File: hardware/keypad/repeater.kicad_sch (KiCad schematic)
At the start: 28 parts, among them Q301 BSS83P, Q302 BSS83P, U301 SN74HCS4075DR, U302 SN74HCS4075DR, U303 SN74HCS4075DR, U304 SN74LVC2G14DBV, U305 LMC555xM, U306 SN74LVC2G14DBVR

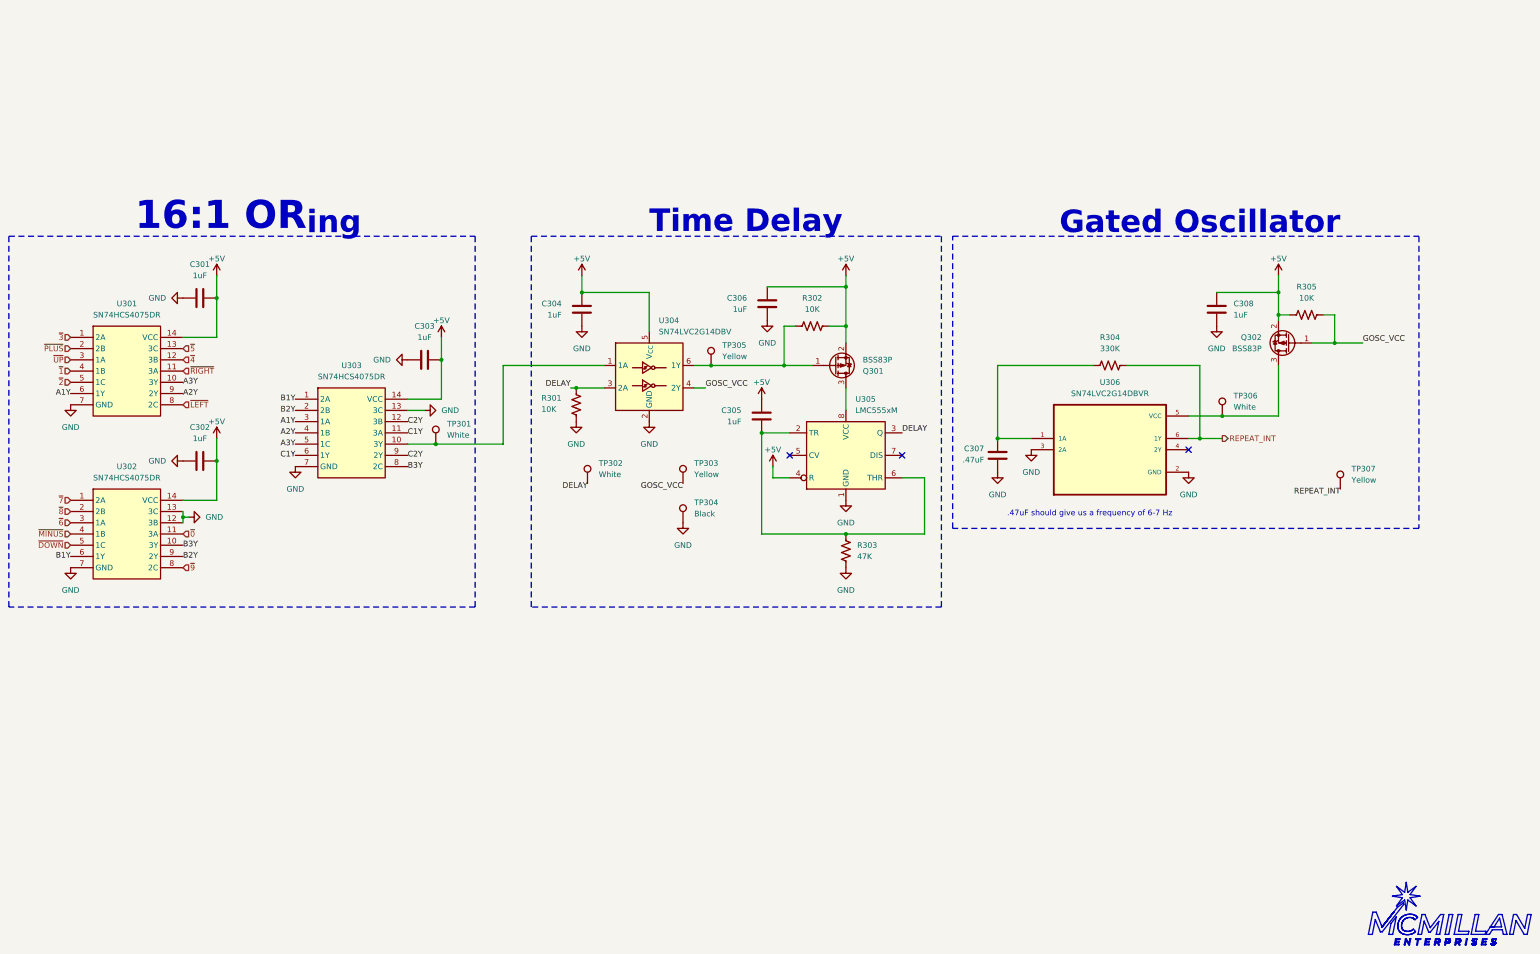
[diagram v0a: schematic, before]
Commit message: Revision X2!
New and improved revision of the keypad! I fixed issues with the repeater and remote SBC power switch circuit (hopefully🤞). I also integrated the Arduino Nano onto the board (ATMEGA328).
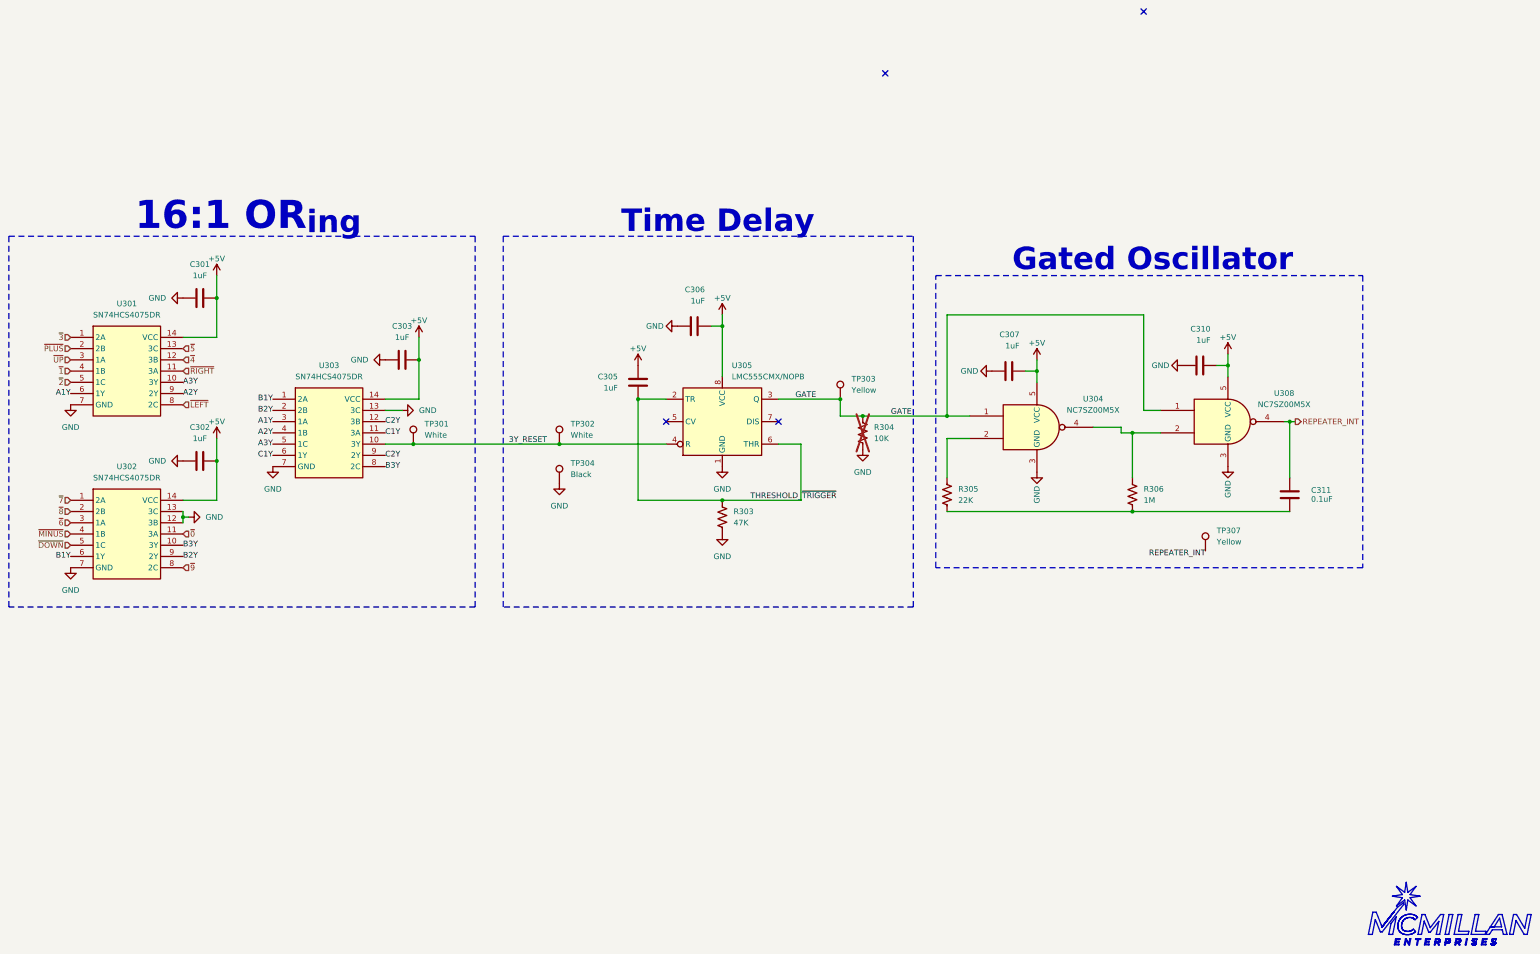
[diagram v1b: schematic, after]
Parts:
- removed C304, C308: 1uF, Capacitor_SMD:C_0805_2012Metric, symbol Device:C
- removed Q301, Q302: BSS83P, Package_TO_SOT_SMD:SOT-23, symbol Transistor_FET:BSS83P
- removed R301, R302: 10K, Resistor_SMD:R_0805_2012Metric, symbol Device:R_US
- removed TP305: Yellow, TestPoint:TestPoint_Keystone_5000-5004_Miniature, symbol Connector:TestPoint
- removed TP306: White, TestPoint:TestPoint_Keystone_5000-5004_Miniature, symbol Connector:TestPoint
- removed U304: SN74LVC2G14DBV, SN74LVC2G14DBVR:SOT95P280X145-6N, symbol 74xGxx:SN74LVC2G14DBV
- removed U306: SN74LVC2G14DBVR, SN74LVC2G14DBVR:SOT95P280X145-6N, symbol SN74LVC2G14DBVR:SN74LVC2G14DBVR
- added C310: 1uF, Capacitor_SMD:C_0805_2012Metric, symbol Device:C
- added C311: 0.1uF, Capacitor_SMD:C_0805_2012Metric, symbol Device:C
- added R306: 1M, Resistor_SMD:R_0805_2012Metric, symbol Device:R_US
- added U304, U308: NC7SZ00M5X, Package_TO_SOT_SMD:SOT-23-5, symbol 74xGxx:74AHC1G00
- C307: value .47uF -> 1uF
- R304: value 330K -> 10K; now not fitted
- R305: value 10K -> 22K
- U305: value LMC555xM -> LMC555CMX/NOPB
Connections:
- net +5V: now also C307.1, U305.8 (VCC), C310.1, U304.5 (VCC), U308.5 (VCC); no longer R305.2, U305.4 (R)
- net GND: now also R304.2, C310.2, U304.3 (GND), U308.3 (GND)
- net 3Y_RESET: now reaches TP301.1, U303.10 (3Y)
- net 3Y_RESET: now also TP302.1, U305.4 (R)
- net THRESHOLD_~{TRIGGER}: now reaches C305.2, R303.1, U305.2 (TR), U305.6 (THR)
- net DELAY renamed GATE
- net GATE: now also R304.1, TP303.1, U304.1, U308.1; no longer TP302.1
- net GOSC_VCC: no longer names the net of R305.1
- net GOSC_VCC: now also U304.2; no longer TP303.1
- net REPEAT_INT renamed REPEATER_INT
- net REPEATER_INT: now also C311.1, U308.4; no longer R304.1
- new net: C311.2, R305.2, R306.2
- new net: R306.1, U304.4, U308.2
- no-connect marks 3 -> 4
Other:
- note removed: ".47uF should give us a frequency of 6-7 Hz"
- moved on the sheet: C303, C305, C306, R303, TP301, TP302, TP303, TP304, TP307, U303, U305
